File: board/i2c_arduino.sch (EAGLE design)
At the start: 20 parts, among them IC1 MEGA8-P

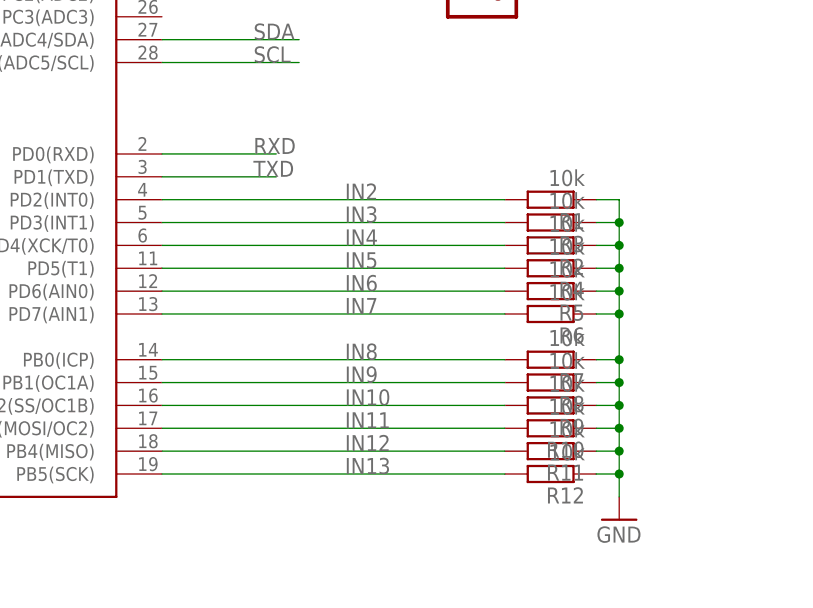
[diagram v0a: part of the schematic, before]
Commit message: Updated buttons handling
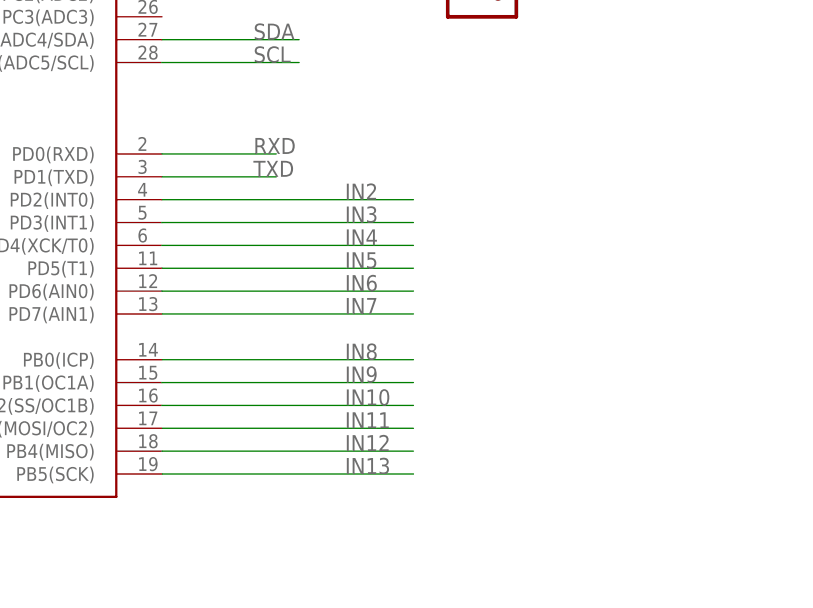
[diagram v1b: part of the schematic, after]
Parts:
- removed R1, R10, R11, R12, R2, R3, R4, R5, R6, R7, R8, R9: 10k, rcl:R-EU_M1206
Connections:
- net GND: no longer R1.1, R10.1, R11.1, R12.1, R2.1, R3.1, R4.1, R5.1, R6.1, R7.1, R8.1, R9.1
- net IN10: no longer R9.2
- net IN11: no longer R10.2
- net IN12: no longer R11.2
- net IN13: no longer R12.2
- net IN2: no longer R1.2
- net IN3: no longer R3.2
- net IN4: no longer R2.2
- net IN5: no longer R4.2
- net IN6: no longer R5.2
- net IN7: no longer R6.2
- net IN8: no longer R7.2
- net IN9: no longer R8.2
